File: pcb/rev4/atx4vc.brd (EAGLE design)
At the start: 69 x 69 mm, 48 parts, among them IC1 MY_7905DT, J2 ATX24RH

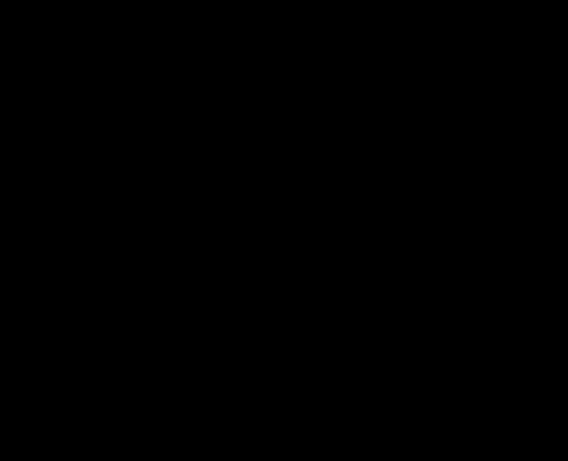
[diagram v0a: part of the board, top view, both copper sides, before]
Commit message: trying out power ic
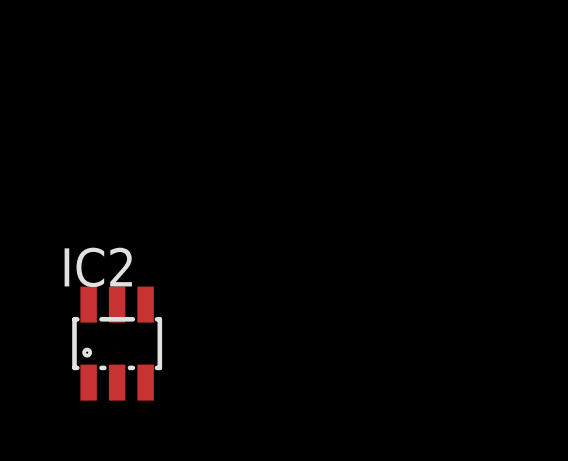
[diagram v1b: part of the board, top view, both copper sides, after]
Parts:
- added IC2: MAX486X/SOT, pmm:SOT23-6
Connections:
- new net VDD: IC2.5
- net GND: now also IC2.2
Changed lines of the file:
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@@
 <grid distance="5" unitdist="mil" unit="mil" style="lines" multiple="1" display="no" altdistance="1" altunitdist="mil" altunit="mil"/>
 <layers>
-<layer number="1" name="Top" color="4" fill="1" visible="no" active="yes"/>
+<layer number="1" name="Top" color="4" fill="1" visible="yes" active="yes"/>
 <layer number="2" name="Route2" color="16" fill="1" visible="no" active="no"/>
 <layer number="3" name="Route3" color="17" fill="1" visible="no" active="no"/>
@@
 <layer number="19" name="Unrouted" color="6" fill="1" visible="yes" active="yes"/>
 <layer number="20" name="Dimension" color="24" fill="1" visible="yes" active="yes"/>
-<layer number="21" name="tPlace" color="7" fill="1" visible="no" active="yes"/>
+<layer number="21" name="tPlace" color="7" fill="1" visible="yes" active="yes"/>
 <layer number="22" name="bPlace" color="7" fill="1" visible="yes" active="yes"/>
-<layer number="23" name="tOrigins" color="15" fill="1" visible="no" active="yes"/>
+<layer number="23" name="tOrigins" color="15" fill="1" visible="yes" active="yes"/>
 <layer number="24" name="bOrigins" color="15" fill="1" visible="yes" active="yes"/>
-<layer number="25" name="tNames" color="7" fill="1" visible="no" active="yes"/>
+<layer number="25" name="tNames" color="7" fill="1" visible="yes" active="yes"/>
 <layer number="26" name="bNames" color="7" fill="1" visible="yes" active="yes"/>
-<layer number="27" name="tValues" color="7" fill="1" visible="no" active="yes"/>
-<layer number="28" name="bValues" color="7" fill="1" visible="no" active="yes"/>
+<layer number="27" name="tValues" color="7" fill="1" visible="yes" active="yes"/>
+<layer number="28" name="bValues" color="7" fill="1" visible="yes" active="yes"/>
 <layer number="29" name="tStop" color="7" fill="3" visible="no" active="yes"/>
 <layer number="30" name="bStop" color="7" fill="6" visible="no" active="yes"/>
@@
 <layer number="37" name="tTest" color="7" fill="1" visible="no" active="yes"/>
 <layer number="38" name="bTest" color="7" fill="1" visible="no" active="yes"/>
-<layer number="39" name="tKeepout" color="4" fill="11" visible="no" active="yes"/>
+<layer number="39" name="tKeepout" color="4" fill="11" visible="yes" active="yes"/>
 <layer number="40" name="bKeepout" color="1" fill="11" visible="yes" active="yes"/>
-<layer number="41" name="tRestrict" color="4" fill="10" visible="no" active="yes"/>
+<layer number="41" name="tRestrict" color="4" fill="10" visible="yes" active="yes"/>
 <layer number="42" name="bRestrict" color="1" fill="10" visible="yes" active="yes"/>
 <layer number="43" name="vRestrict" color="2" fill="10" visible="no" active="yes"/>
@@
 <layer number="49" name="Reference" color="7" fill="1" visible="no" active="yes"/>
 <layer number="50" name="dxf" color="7" fill="1" visible="no" active="no"/>
-<layer number="51" name="tDocu" color="7" fill="1" visible="no" active="yes"/>
+<layer number="51" name="tDocu" color="7" fill="1" visible="yes" active="yes"/>
 <layer number="52" name="bDocu" color="7" fill="1" visible="yes" active="yes"/>
 <layer number="53" name="tGND_GNDA" color="7" fill="1" visible="no" active="no"/>
@@
 <layer number="154" name="FabDoc2" color="7" fill="1" visible="no" active="yes"/>
 <layer number="155" name="FabDoc3" color="7" fill="1" visible="no" active="yes"/>
+<layer number="156" name="gesam-Maß" color="7" fill="1" visible="yes" active="yes"/>
+<layer number="157" name="FaceMchng" color="7" fill="1" visible="yes" active="yes"/>
+<layer number="158" name="FaceMMeas" color="7" fill="1" visible="yes" active="yes"/>
+<layer number="159" name="Geh-Bear2" color="7" fill="1" visible="yes" active="yes"/>
+<layer number="160" name="O_Dim" color="7" fill="1" visible="yes" active="yes"/>
+<layer number="161" name="tomplace2" color="7" fill="1" visible="yes" active="yes"/>
 <layer number="166" name="AntennaArea" color="7" fill="1" visible="no" active="yes"/>
 <layer number="168" name="4mmHeightArea" color="7" fill="1" visible="no" active="yes"/>
@@
 <layer number="250" name="Descript" color="3" fill="1" visible="no" active="no"/>
 <layer number="251" name="SMDround" color="12" fill="11" visible="no" active="no"/>
+<layer number="252" name="BR-BS" color="7" fill="1" visible="yes" active="yes"/>
 <layer number="253" name="Extra" color="7" fill="1" visible="no" active="yes"/>
 <layer number="254" name="cooling" color="7" fill="1" visible="no" active="yes"/>
@@
 </element>
 <element name="JP1" library="appleii" package="1X04" value="" x="24.892" y="58.674" smashed="yes" rot="R180"/>
+<element name="IC2" library="pmm" package="SOT23-6" value="MAX486X/SOT" x="-20.193" y="-4.191" smashed="yes">
+<attribute name="NAME" x="-22.098" y="-2.286" size="1.27" layer="25"/>
+<attribute name="VALUE" x="-22.098" y="-7.62" size="1.27" layer="27"/>
+</element>
 </elements>
 <signals>
@@
 <wire x1="39.624" y1="56.7245" x2="39.624" y2="58.674" width="1.524" layer="16"/>
 <wire x1="41.2195" y1="55.129" x2="39.624" y2="56.7245" width="1.524" layer="16"/>
+<contactref element="IC2" pad="2"/>
+<wire x1="52.9035" y1="53.359" x2="55.0735" y2="52.459" width="0" layer="19" extent="1-16"/>
+<wire x1="52.5115" y1="45.091" x2="53.2735" y2="50.679" width="0" layer="19" extent="1-1"/>
+<wire x1="52.5115" y1="39.376" x2="52.5115" y2="45.091" width="0" layer="19" extent="1-1"/>
+<wire x1="54.2985" y1="29.311" x2="52.5115" y2="39.376" width="0" layer="19" extent="1-1"/>
+<wire x1="48.3205" y1="19.947" x2="54.3025" y2="27.093" width="0" layer="19" extent="1-1"/>
+<wire x1="53.7925" y1="16.01" x2="48.3205" y2="19.947" width="0" layer="19" extent="1-1"/>
+<wire x1="61.3485" y1="16.314" x2="62.2635" y2="17.409" width="0" layer="19" extent="1-1"/>
+<wire x1="61.3485" y1="9.864" x2="62.2635" y2="8.769" width="0" layer="19" extent="1-16"/>
+<wire x1="41.4475" y1="15.508" x2="48.3205" y2="19.947" width="0" layer="19" extent="1-1"/>
+<wire x1="39.6845" y1="22.485" x2="41.4475" y2="15.508" width="0" layer="19" extent="1-1"/>
+<wire x1="28.702" y1="58.674" x2="39.624" y2="58.674" width="0" layer="19" extent="1-1"/>
+<wire x1="29.5355" y1="13.84" x2="41.4475" y2="15.508" width="0" layer="19" extent="1-1"/>
+<wire x1="16.6965" y1="57.6" x2="28.702" y2="58.674" width="0" layer="19" extent="1-1"/>
+<wire x1="32.9535" y1="45.066" x2="41.2195" y2="55.129" width="0" layer="19" extent="16-16"/>
+<wire x1="32.9535" y1="43.442" x2="32.9535" y2="45.066" width="0" layer="19" extent="16-16"/>
+<wire x1="32.3295" y1="41.918" x2="32.9535" y2="43.442" width="0" layer="19" extent="16-16"/>
+<wire x1="30.0435" y1="42.451" x2="32.3295" y2="41.918" width="0" layer="19" extent="16-16"/>
+<wire x1="30.9295" y1="38.616" x2="32.3295" y2="41.918" width="0" layer="19" extent="16-16"/>
+<wire x1="31.8565" y1="36.076" x2="30.9295" y2="38.616" width="0" layer="19" extent="16-16"/>
+<wire x1="31.8565" y1="34.425" x2="31.8565" y2="36.076" width="0" layer="19" extent="16-16"/>
+<wire x1="16.6965" y1="19.8" x2="29.5355" y2="13.84" width="0" layer="19" extent="1-1"/>
+<wire x1="16.6965" y1="36.6" x2="11.1965" y2="36.6" width="0" layer="19" extent="1-1"/>
+<wire x1="16.6965" y1="32.4" x2="16.6965" y2="36.6" width="0" layer="19" extent="1-1"/>
+<wire x1="16.6965" y1="28.2" x2="16.6965" y2="32.4" width="0" layer="19" extent="1-1"/>
+<wire x1="-20.193" y1="-5.491" x2="11.1965" y2="19.8" width="0" layer="19" extent="1-1"/>
 </signal>
 <signal name="N$5">
@@
 <wire x1="59.5175" y1="11" x2="59.5175" y2="11.6" width="0.2032" layer="16"/>
 </signal>
+<signal name="VDD">
+<contactref element="IC2" pad="5"/>
+</signal>
 </signals>

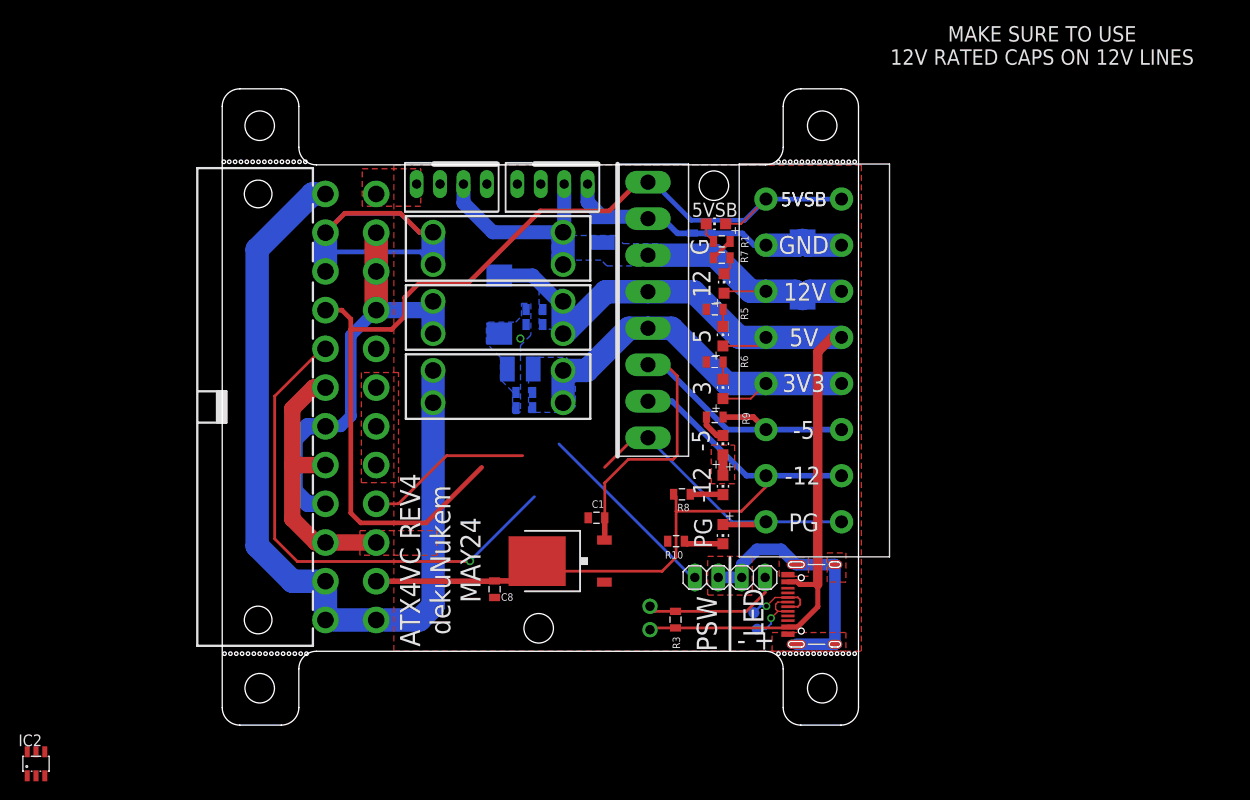
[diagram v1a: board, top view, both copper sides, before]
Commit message: trying out power ic
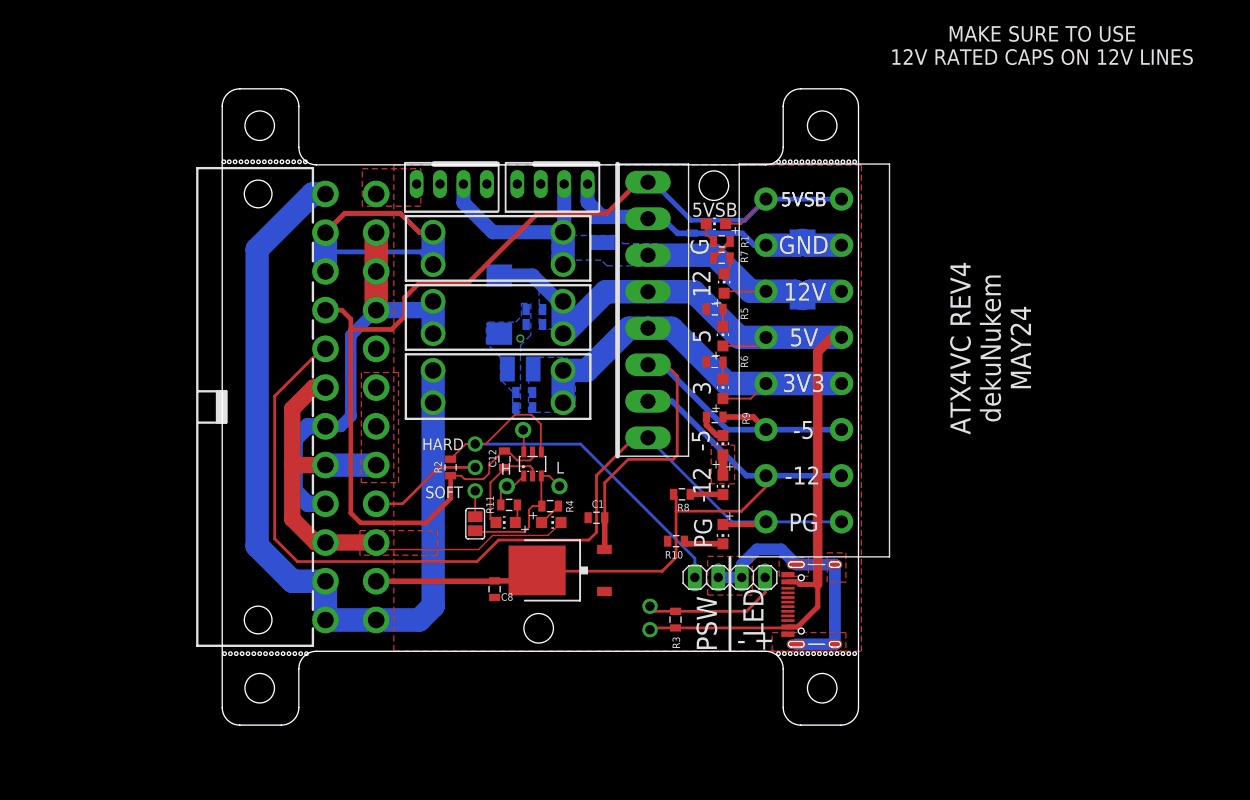
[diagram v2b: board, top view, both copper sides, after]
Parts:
- removed TP1, TP2: TPTP12R, testpad:TP12R
- added C12: 100nF, atx_power_control:0805$1
- added JP3, JP6, JP8: (no value), adafruit_changed:1X01-CLEANBIG
- added JP7: (no value), adafruit_changed:1X03-CLEANBIG
- added LED8, LED9: (no value), adafruit:CHIP-LED0805
- added R11, R2, R4: 5K1, atx_power_control:0805
- added SJ1: (no value), jumper:SJ
- moved IC2 62.9 mm to (33.7, 28.3)
- moved IC1 1.02 mm to (36.6, 16.8)
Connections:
- removed net N$2: J1.A6, J1.B6, TP2.TP
- removed net N$4: J1.A7, J1.B7, TP1.TP
- removed net VDD: IC2.5
- new net N$12: IC2.4, JP4.2, JP7.3, R2.2
- new net N$13: LED8.A, R4.1
- new net N$16: LED9.A, R11.1
- new net N$19: IC2.3, JP8.1, R4.2, SJ1.2
- new net N$3: IC2.6, JP3.1
- new net N$6: JP7.1, SJ1.1
- new net N$7: IC2.1, JP6.1, R11.2
- net GND: now also C12.1, LED8.C, LED9.C
- net N$15: now also JP7.2; no longer JP4.2
- net VCC: now also C12.2, IC2.5, R2.1
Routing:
- net N$12: track 0.00 -> 46.3 mm
- net GND: track 98.6 -> 136.7 mm
- net N$15: track 38.8 -> 12.4 mm
- net N$19: track 0.00 -> 15.3 mm
- net N$11: track 90.8 -> 103.3 mm, vias 1 -> 0
- net VCC: track 110.5 -> 120.2 mm
- net N$2: track 7.89 -> 0.00 mm, vias 1 -> 0
- net N$4: track 6.78 -> 0.00 mm, vias 1 -> 0
- net N$7: track 0.00 -> 4.60 mm
- net N$6: track 0.00 -> 2.79 mm
- net N$13: track 0.00 -> 2.56 mm
- net N$3: track 0.00 -> 2.41 mm
- net N$16: track 0.00 -> 2.00 mm
- net -5V: track 56.7 -> 57.7 mm
- net -12V: track 77.8 -> 77.0 mm
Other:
- board text added: "H"
- board text added: "HARD"
- board text added: "L"
- board text added: "SOFT"
